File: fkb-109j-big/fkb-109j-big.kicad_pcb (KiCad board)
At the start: 2 copper layers, 260 parts

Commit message: continue layout
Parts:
- added MX_KPPLS2: MX-NoLED, Alps_Only:ALPS-2U, F.Cu at (602.5, 76.2)
- moved MX_KP1 264.0 mm to (545.3, 104.8)
- moved MX_KP2 264.0 mm to (564.4, 104.8)
- moved MX_KP3 264.0 mm to (583.4, 104.8)
- moved MX_KP7 264.0 mm to (545.3, 66.7)
- moved MX_KP8 264.0 mm to (564.4, 66.7)
- moved MX_KP9 264.0 mm to (583.4, 66.7)
- moved MX_KPDOT1 264.0 mm to (583.4, 123.8)
- moved MX_KPEQ1 264.0 mm to (564.4, 47.6)
- moved MX_KPFSL1 264.0 mm to (583.4, 47.6)
- moved MX_NMLK1 264.0 mm to (545.3, 47.6)
- moved MX_KP0 264.0 mm to (554.8, 123.8)
- moved MX_KP4 264.0 mm to (545.3, 85.7)
- moved MX_KP5 264.0 mm to (564.4, 85.7)
- moved MX_KP6 264.0 mm to (583.4, 85.7)
- moved MX_KPAST1 264.0 mm to (602.5, 47.6)
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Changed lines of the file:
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@@
   )
   (footprint "Alps_Only:ALPS-1U" (layer "F.Cu")
-    (at 438.15 -193.675)
+    (at 545.30625 47.625)
     (property "Sheetfile" "fkb-109j-big.kicad_sch")
     (property "Sheetname" "")
@@
   )
   (footprint "Alps_Only:ALPS-1U" (layer "F.Cu")
-    (at 444.5 80.9625)
+    (at 433.8955 80.9625)
     (property "Sheetfile" "fkb-109j-big.kicad_sch")
     (property "Sheetname" "")
@@
   )
   (footprint "Alps_Only:ALPS-1U" (layer "F.Cu")
-    (at 457.2 -174.625)
+    (at 564.35625 66.675)
     (property "Sheetfile" "fkb-109j-big.kicad_sch")
     (property "Sheetname" "")
@@
   )
   (footprint "Alps_Only:ALPS-1U" (layer "F.Cu")
-    (at 476.25 -136.525)
+    (at 583.40625 104.775)
     (property "Sheetfile" "fkb-109j-big.kicad_sch")
     (property "Sheetname" "")
@@
   )
   (footprint "Alps_Only:ALPS-1U" (layer "F.Cu")
-    (at 476.25 -174.625)
+    (at 583.40625 66.675)
     (property "Sheetfile" "fkb-109j-big.kicad_sch")
     (property "Sheetname" "")
@@
   )
   (footprint "Alps_Only:ALPS-1U" (layer "F.Cu")
-    (at 482.71875 138.14375)
+    (at 471.9955 138.1125)
     (property "Sheetfile" "fkb-109j-big.kicad_sch")
     (property "Sheetname" "")
@@
   )
   (footprint "Alps_Only:ALPS-1U" (layer "F.Cu")
-    (at 457.2 -193.675)
+    (at 564.35625 47.625)
     (property "Sheetfile" "fkb-109j-big.kicad_sch")
     (property "Sheetname" "")
@@
   )
   (footprint "Alps_Only:ALPS-1U" (layer "F.Cu")
-    (at 438.15 -136.525)
+    (at 545.30625 104.775)
     (property "Sheetfile" "fkb-109j-big.kicad_sch")
     (property "Sheetname" "")
@@
   )
   (footprint "Alps_Only:ALPS-1U" (layer "F.Cu")
-    (at 457.2 -136.525)
+    (at 564.35625 104.775)
     (property "Sheetfile" "fkb-109j-big.kicad_sch")
     (property "Sheetname" "")
@@
   )
   (footprint "Alps_Only:ALPS-1U" (layer "F.Cu")
-    (at 476.25 -117.475)
+    (at 583.40625 123.825)
     (property "Sheetfile" "fkb-109j-big.kicad_sch")
     (property "Sheetname" "")
@@
   )
   (footprint "Alps_Only:ALPS-1U" (layer "F.Cu")
-    (at 444.5 61.9125)
+    (at 433.8955 61.9125)
     (property "Sheetfile" "fkb-109j-big.kicad_sch")
     (property "Sheetname" "")
@@
   )
   (footprint "Alps_Only:ALPS-1U" (layer "F.Cu")
-    (at 463.55 80.9625)
+    (at 452.9455 80.9625)
     (property "Sheetfile" "fkb-109j-big.kicad_sch")
     (property "Sheetname" "")
@@
   )
   (footprint "Alps_Only:ALPS-1U" (layer "F.Cu")
-    (at 438.15 -174.625)
+    (at 545.30625 66.675)
     (property "Sheetfile" "fkb-109j-big.kicad_sch")
     (property "Sheetname" "")
@@
   )
   (footprint "Alps_Only:ALPS-2U" (layer "F.Cu")
-    (at 425.45 90.4875 -90)
+    (at 401.6375 109.5375 -90)
     (property "Sheetfile" "fkb-109j-big.kicad_sch")
     (property "Sheetname" "")
@@
   )
   (footprint "Alps_Only:ALPS-1U" (layer "F.Cu")
-    (at 463.66875 138.14375)
+    (at 452.9455 138.1125)
     (property "Sheetfile" "fkb-109j-big.kicad_sch")
     (property "Sheetname" "")
@@
   )
   (footprint "Alps_Only:ALPS-1U" (layer "F.Cu")
-    (at 476.25 -155.575)
+    (at 583.40625 85.725)
     (property "Sheetfile" "fkb-109j-big.kicad_sch")
     (property "Sheetname" "")
@@
     )
   )
+  (footprint "Alps_Only:ALPS-2U" (layer "F.Cu")
+    (at 602.45625 76.2 -90)
+    (property "Sheetfile" "fkb-109j-big.kicad_sch")
+    (property "Sheetname" "")
+    (attr through_hole)
+    (fp_text reference "MX_KPPLS2" (at 0 3.175 90) (layer "Dwgs.User")
+        (effects (font (size 1 1) (thickness 0.15)))
+    )
+    (fp_text value "MX-NoLED" (at 0 -7.9375 90) (layer "Dwgs.User")
+        (effects (font (size 1 1) (thickness 0.15)))
+    )
+    (fp_line (start -19.05 -9.525) (end 19.05 -9.525)
+      (stroke (width 0.15) (type solid)) (layer "Dwgs.User"))
+    (fp_line (start -19.05 9.525) (end -19.05 -9.525)
+      (stroke (width 0.15) (type solid)) (layer "Dwgs.User"))
+    (fp_line (start -19.05 9.525) (end 19.05 9.525)
+      (stroke (width 0.15) (type solid)) (layer "Dwgs.User"))
+    (fp_line (start -7 -7) (end -7 -5)
+      (stroke (width 0.15) (type solid)) (layer "Dwgs.User"))
+    (fp_line (start -7 5) (end -7 7)
+      (stroke (width 0.15) (type solid)) (layer "Dwgs.User"))
+    (fp_line (start -7 7) (end -5 7)
+      (stroke (width 0.15) (type solid)) (layer "Dwgs.User"))
+    (fp_line (start -5 -7) (end -7 -7)
+      (stroke (width 0.15) (type solid)) (layer "Dwgs.User"))
+    (fp_line (start 5 -7) (end 7 -7)
+      (stroke (width 0.15) (type solid)) (layer "Dwgs.User"))
+    (fp_line (start 5 7) (end 7 7)
+      (stroke (width 0.15) (type solid)) (layer "Dwgs.User"))
+    (fp_line (start 7 -7) (end 7 -5)
+      (stroke (width 0.15) (type solid)) (layer "Dwgs.User"))
+    (fp_line (start 7 7) (end 7 5)
+      (stroke (width 0.15) (type solid)) (layer "Dwgs.User"))
+    (fp_line (start 19.05 -9.525) (end 19.05 9.525)
+      (stroke (width 0.15) (type solid)) (layer "Dwgs.User"))
+    (pad "1" thru_hole circle (at -2.5 -4 270) (size 2.25 2.25) (drill 1.47) (layers "*.Cu" "B.Mask")
+      (net 160 "COL20") (pinfunction "COL") (pintype "passive"))
+    (pad "2" thru_hole circle (at 2.5 -4.5 270) (size 2.25 2.25) (drill 1.47) (layers "*.Cu" "B.Mask")
+      (net 126 "Net-(D111-A)") (pinfunction "ROW") (pintype "passive"))
+  )
   (footprint "Alps_Only:ALPS-1U" (layer "F.Cu")
     (at 173.0375 100.0125)
@@
   )
   (footprint "Alps_Only:ALPS-1U" (layer "F.Cu")
-    (at 457.2 -155.575)
+    (at 564.35625 85.725)
     (property "Sheetfile" "fkb-109j-big.kicad_sch")
     (property "Sheetname" "")
@@
   )
   (footprint "Alps_Only:ALPS-1U" (layer "F.Cu")
-    (at 463.66875 119.09375)
+    (at 452.9455 119.0625)
     (property "Sheetfile" "fkb-109j-big.kicad_sch")
     (property "Sheetname" "")
@@
   )
   (footprint "Alps_Only:ALPS-1U" (layer "F.Cu")
-    (at 463.55 61.9125)
+    (at 452.9455 61.9125)
     (property "Sheetfile" "fkb-109j-big.kicad_sch")
     (property "Sheetname" "")
@@
   )
   (footprint "Alps_Only:ALPS-1U" (layer "F.Cu")
-    (at 476.25 -193.675)
+    (at 583.40625 47.625)
     (property "Sheetfile" "fkb-109j-big.kicad_sch")
     (property "Sheetname" "")
@@
   )
   (footprint "Alps_Only:ALPS-1U" (layer "F.Cu")
-    (at 482.6 80.9625)
+    (at 471.9955 80.9625)
     (property "Sheetfile" "fkb-109j-big.kicad_sch")
     (property "Sheetname" "")
@@
   )
   (footprint "Alps_Only:ALPS-1U" (layer "F.Cu")
-    (at 495.3 -155.575)
+    (at 602.45625 85.725)
     (property "Sheetfile" "fkb-109j-big.kicad_sch")
     (property "Sheetname" "")
@@
   )
   (footprint "Alps_Only:ALPS-1U" (layer "F.Cu")
-    (at 482.6 61.9125)
+    (at 471.9955 61.9125)
     (property "Sheetfile" "fkb-109j-big.kicad_sch")
     (property "Sheetname" "")
@@
   )
   (footprint "Alps_Only:ALPS-1U" (layer "F.Cu")
-    (at 495.3 -193.675)
+    (at 602.45625 47.625)
     (property "Sheetfile" "fkb-109j-big.kicad_sch")
     (property "Sheetname" "")
@@
   )
   (footprint "Alps_Only:ALPS-2U" (layer "F.Cu")
-    (at 447.675 -117.475)
+    (at 554.83125 123.825)
     (property "Sheetfile" "fkb-109j-big.kicad_sch")
     (property "Sheetname" "")
@@
   )
   (footprint "Alps_Only:ALPS-2U" (layer "F.Cu")
-    (at 495.3 -127 -90)
+    (at 602.45625 114.3 -90)
     (property "Sheetfile" "fkb-109j-big.kicad_sch")
     (property "Sheetname" "")
@@
   )
   (footprint "Alps_Only:ALPS-1U" (layer "F.Cu")
-    (at 438.15 -155.575)
+    (at 545.30625 85.725)
     (property "Sheetfile" "fkb-109j-big.kicad_sch")
     (property "Sheetname" "")
@@
   )
   (footprint "Alps_Only:ALPS-1U" (layer "F.Cu")
-    (at 495.3 -174.625)
+    (at 602.45625 66.675)
     (property "Sheetfile" "fkb-109j-big.kicad_sch")
     (property "Sheetname" "")
@@
   )
   (footprint "Alps_Only:ALPS-1U" (layer "F.Cu")
-    (at 444.61875 138.14375)
+    (at 433.8955 138.1125)
     (property "Sheetfile" "fkb-109j-big.kicad_sch")
     (property "Sheetname" "")
@@
     )
   )
+  (dimension (type aligned) (layer "Dwgs.User")
+    (pts (xy 415.925 128.5875) (xy 424.3705 128.5875))
+    (height 0)
+    (gr_text "8.4455 mm" (at 420.14775 127.4375) (layer "Dwgs.User")
+      (effects (font (size 1 1) (thickness 0.15)))
+    )
+    (format (prefix "") (suffix "") (units 3) (units_format 1) (precision 4))
+    (style (thickness 0.15) (arrow_length 1.27) (text_position_mode 0) (extension_height 0.58642) (extension_offset 0.5) keep_text_aligned)
+  )
+  (dimension (type aligned) (layer "Dwgs.User")
+    (pts (xy 424.3705 147.6375) (xy 443.4205 147.6375))
+    (height 8.73125)
+    (gr_text "19.0500 mm" (at 433.8955 155.21875) (layer "Dwgs.User")
+      (effects (font (size 1 1) (thickness 0.15)))
+    )
+    (format (prefix "") (suffix "") (units 3) (units_format 1) (precision 4))
+    (style (thickness 0.15) (arrow_length 1.27) (text_position_mode 0) (extension_height 0.58642) (extension_offset 0.5) keep_text_aligned)
+  )
+  (dimension (type aligned) (layer "Dwgs.User")
+    (pts (xy 415.925 90.4875) (xy 424.3705 90.4875))
+    (height 0)
+    (gr_text "8.4455 mm" (at 420.14775 89.3375) (layer "Dwgs.User")
+      (effects (font (size 1 1) (thickness 0.15)))
+    )
+    (format (prefix "") (suffix "") (units 3) (units_format 1) (precision 4))
+    (style (thickness 0.15) (arrow_length 1.27) (text_position_mode 0) (extension_height 0.58642) (extension_offset 0.5) keep_text_aligned)
+  )
+  (dimension (type aligned) (layer "Dwgs.User")
+    (pts (xy 443.4205 90.4875) (xy 443.4205 109.5375))
+    (height -9.525)
+    (gr_text "19.0500 mm" (at 451.7955 100.0125 90) (layer "Dwgs.User")
+      (effects (font (size 1 1) (thickness 0.15)))
+    )
+    (format (prefix "") (suffix "") (units 3) (units_format 1) (precision 4))
+    (style (thickness 0.15) (arrow_length 1.27) (text_position_mode 0) (extension_height 0.58642) (extension_offset 0.5) keep_text_aligned)
+  )
   (segment (start 144.58125 133.6125) (end 146.9625 133.6125) (width 0.25) (layer "F.Cu") (net 24))

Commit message: finish preliminary layout
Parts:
- added MX_ESC2: MX-NoLED, Alps_Only:ALPS-1U, F.Cu at (139.7, 38.1)
- added MX_F14: MX-NoLED, Alps_Only:ALPS-1U, F.Cu at (177.8, 38.1)
- added MX_F15: MX-NoLED, Alps_Only:ALPS-1U, F.Cu at (196.8, 38.1)
- added MX_F16: MX-NoLED, Alps_Only:ALPS-1U, F.Cu at (215.9, 38.1)
- added MX_F17: MX-NoLED, Alps_Only:ALPS-1U, F.Cu at (234.9, 38.1)
- added MX_F18: MX-NoLED, Alps_Only:ALPS-1U, F.Cu at (263.5, 38.1)
- added MX_F19: MX-NoLED, Alps_Only:ALPS-1U, F.Cu at (282.6, 38.1)
- added MX_F20: MX-NoLED, Alps_Only:ALPS-1U, F.Cu at (301.6, 38.1)
- added MX_F21: MX-NoLED, Alps_Only:ALPS-1U, F.Cu at (320.7, 38.1)
- added MX_F22: MX-NoLED, Alps_Only:ALPS-1U, F.Cu at (349.2, 38.1)
- added MX_F23: MX-NoLED, Alps_Only:ALPS-1U, F.Cu at (368.3, 38.1)
- added MX_F24: MX-NoLED, Alps_Only:ALPS-1U, F.Cu at (387.4, 38.1)
- added MX_F25: MX-NoLED, Alps_Only:ALPS-1U, F.Cu at (406.4, 38.1)
- added MX_PSBRK2: MX-NoLED, Alps_Only:ALPS-1U, F.Cu at (473.1, 38.1)
- added MX_PSCRN2: MX-NoLED, Alps_Only:ALPS-1U, F.Cu at (435.0, 38.1)
- added MX_SCRLK2: MX-LED, Alps_Only:ALPS-1U, F.Cu at (454.0, 38.1)
- moved MX_PSBRK1 110.7 mm to (473.1, 38.1)
- moved MX_F9 83.2 mm to (349.2, 38.1), turned to 0 degrees
- moved MX_F10 82.0 mm to (368.3, 38.1), turned to 0 degrees
- moved MX_F11 80.9 mm to (387.4, 38.1), turned to 0 degrees
- moved MX_F12 79.8 mm to (406.4, 38.1), turned to 0 degrees
- moved MX_F5 78.4 mm to (263.5, 38.1), turned to 0 degrees
- moved MX_F6 77.2 mm to (282.6, 38.1), turned to 0 degrees
- moved MX_F7 76.1 mm to (301.6, 38.1), turned to 0 degrees
- moved MX_F8 75.0 mm to (320.7, 38.1), turned to 0 degrees
- moved MX_PSCRN1 67.6 mm to (435.0, 38.1)
- moved MX_SCRLK1 66.5 mm to (454.0, 38.1)
- moved MX_KP1 45.9 mm to (501.6, 119.1)
- moved MX_KP2 45.9 mm to (520.7, 119.1)
- moved MX_KP3 45.9 mm to (539.8, 119.1)
- moved MX_KP4 45.9 mm to (501.6, 100.0)
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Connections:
- MX_RSHFT1 pad 1: COL12 -> Net-(D77-A)
- MX_RSHFT1 pad 2: Net-(D77-A) -> COL12
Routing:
- net Net-(D4-A): track 0.00 -> 9.69 mm
- net Net-(D3-A): track 0.00 -> 9.69 mm
- net Net-(D2-A): track 0.00 -> 9.69 mm
- net Net-(D1-A): track 0.00 -> 9.69 mm
- net Net-(MX_F17-ROW): track 0.00 -> 2.62 mm
- net Net-(MX_F16-ROW): track 0.00 -> 2.62 mm
- net Net-(MX_F15-ROW): track 0.00 -> 2.62 mm
- net Net-(MX_F1-COL): track 0.00 -> 2.62 mm
- net Net-(MX_ESC1-COL): track 0.00 -> 2.62 mm
- net Net-(D25-A): track 0.00 -> 0.50 mm

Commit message: start moving diodes
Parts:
- added MX_BSLSH2: MX-NoLED, Alps_Only:ALPS-1U, F.Cu at (163.5, 119.1)
- added MX_LSHFT2: MX-NoLED, Alps_Only:ALPS-1.25U, F.Cu at (142.1, 119.1)
- moved D1 539.0 mm to (149.2, 47.5), turned to 90 degrees
- moved D5 537.0 mm to (149.2, 71.3), turned to 90 degrees
- moved D6 519.1 mm to (168.3, 71.3), turned to 90 degrees
- moved D2 502.6 mm to (187.3, 47.5), turned to 90 degrees
- moved D7 501.3 mm to (187.3, 71.3), turned to 90 degrees
- moved D3 485.0 mm to (206.4, 47.5), turned to 90 degrees
- moved D100 478.3 mm to (252.4, 202.0)
- moved D101 478.3 mm to (252.4, 205.5)
- moved D102 478.3 mm to (252.4, 209.1)
- moved D103 478.3 mm to (252.4, 212.6)
- moved D104 478.3 mm to (252.4, 216.2)
- moved D105 478.3 mm to (252.4, 219.7)
- moved D106 478.3 mm to (252.4, 223.3)
- moved D107 478.3 mm to (252.4, 226.8)
- moved D108 478.3 mm to (252.4, 230.4)
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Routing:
- net COL0: track 2.38 -> 52.2 mm
- net Net-(D17-A): track 0.00 -> 11.1 mm
- net Net-(D4-A): track 9.69 -> 0.50 mm
- net Net-(D3-A): track 9.69 -> 0.50 mm
- net Net-(D2-A): track 9.69 -> 0.50 mm
- net Net-(D1-A): track 9.69 -> 0.50 mm
- net Net-(D10-A): track 0.00 -> 2.38 mm

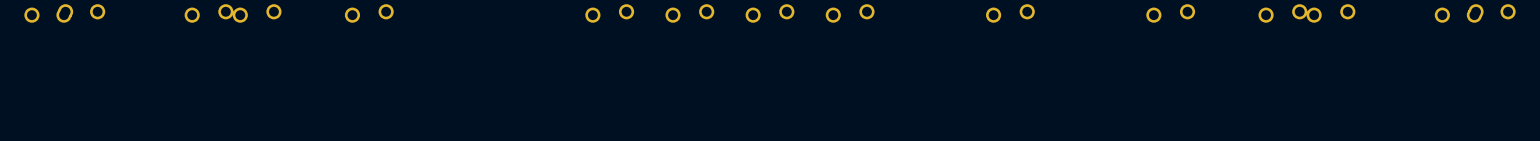
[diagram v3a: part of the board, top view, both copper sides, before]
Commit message: add 7u/jis bottom-row
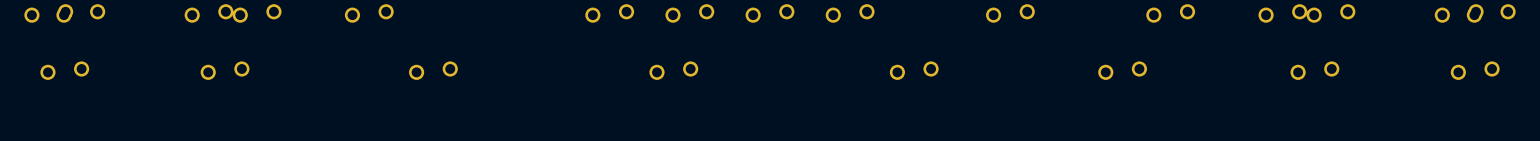
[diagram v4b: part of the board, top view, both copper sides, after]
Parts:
- added MX_KC1: MX-NoLED, Alps_Only:ALPS-1.5U, F.Cu at (325.4, 138.1)
- added MX_KC2: MX-NoLED, Alps_Only:ALPS-1.75U, F.Cu at (294.5, 138.1)
- added MX_KC7B2: MX-NoLED, Alps_Only:ALPS-1.75U, F.Cu at (223.0, 138.1)
- added MX_LALT2: MX-NoLED, Alps_Only:ALPS-1.5U, F.Cu at (192.1, 138.1)
- added MX_LWIN2: MX-NoLED, Alps_Only:ALPS-1U, F.Cu at (168.3, 138.1)
- added MX_RALT2: MX-NoLED, Alps_Only:ALPS-1.5U, F.Cu at (354.0, 138.1)
- added MX_RWIN2: MX-NoLED, Alps_Only:ALPS-1U, F.Cu at (377.8, 138.1)
- added MX_SPACE5: MX-NoLED, Alps_Only:ALPS-2U, F.Cu at (258.8, 138.1)

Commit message: continue placing diodes
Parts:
- moved D42 221.1 mm to (292.1, 46.7), turned to 90 degrees
- moved D54 211.1 mm to (330.2, 46.7), turned to 90 degrees
- moved D36 194.4 mm to (273.1, 46.7), turned to 90 degrees
- moved D37 192.5 mm to (263.5, 70.5), turned to 90 degrees
- moved D75 184.0 mm to (414.3, 127.6), turned to 90 degrees
- moved D48 183.1 mm to (311.1, 46.7), turned to 90 degrees
- moved D49 179.5 mm to (301.6, 70.5), turned to 90 degrees
- moved D50 170.7 mm to (311.1, 89.5), turned to 90 degrees
- moved D31 167.2 mm to (244.5, 70.5), turned to 90 degrees
- moved D30 166.2 mm to (244.5, 46.7), turned to 90 degrees
- moved D52 154.8 mm to (325.4, 127.6), turned to 90 degrees
- moved D32 154.5 mm to (254.0, 89.5), turned to 90 degrees
- moved D20 152.5 mm to (215.9, 89.5), turned to 90 degrees
- moved D43 152.0 mm to (282.6, 70.5), turned to 90 degrees
- moved D51 150.0 mm to (296.9, 108.6), turned to 90 degrees
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- renumbered D19 to D10, D87 to D100, D88 to D101, D89 to D102, D94 to D103, D95 to D104, D100 to D105, D109 to D108, D110 to D109, D20 to D11, D111 to D110, D112 to D111, D2 to D12, D7 to D13, D13 to D14, D14 to D15, D21 to D16, D22 to D17, D3 to D18, D8 to D19, D5 to D2, D15 to D20, D16 to D21, D23 to D22, D24 to D23, D4 to D24, D26 to D25, D27 to D26, D28 to D27, D29 to D28, D30 to D29, D9 to D3, D25 to D30, D32 to D31, D33 to D32, D34 to D33, D35 to D34, D36 to D35, D31 to D36, D38 to D37, D39 to D38, D40 to D39, D10 to D4, D41 to D40, D42 to D41, D37 to D42, D44 to D43, D45 to D44, D46 to D45, D47 to D46, D48 to D47, D43 to D48, D50 to D49, D17 to D5, D51 to D50, D52 to D51, D53 to D52, D54 to D53, D49 to D54, D56 to D55, D57 to D56, D58 to D57, D59 to D58, D60 to D59, D18 to D6, D55 to D60, D62 to D61, D63 to D62, D64 to D63, D65 to D64, D66 to D65, D61 to D66, D68 to D67, D69 to D68, D70 to D69, D6 to D7, D71 to D70, D67 to D71, D74 to D72, D75 to D73, D76 to D74, D77 to D75, D73 to D76, D79 to D77, D72 to D79, D11 to D8, D82 to D80, D91 to D81, D92 to D82, D93 to D83, D96 to D84, D97 to D85, D98 to D86, D99 to D87, D101 to D88, D102 to D89, D12 to D9, D103 to D90, D104 to D91, D105 to D92, D108 to D93, D80 to D94, D81 to D95, D83 to D96, D84 to D97, D85 to D98, D86 to D99

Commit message: finish preliminary diode placement.
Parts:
- moved D108 355.0 mm to (567.5, 70.5), turned to 90 degrees
- moved D103 354.6 mm to (548.5, 70.3), turned to 90 degrees
- moved D109 348.8 mm to (568.3, 89.5), turned to 90 degrees
- moved D104 347.7 mm to (549.3, 89.5), turned to 90 degrees
- moved D110 342.6 mm to (568.3, 108.4), turned to 90 degrees
- moved D111 329.2 mm to (566.7, 146.5), turned to 90 degrees
- moved D99 326.6 mm to (530.2, 70.3), turned to 90 degrees
- moved D100 319.6 mm to (530.2, 89.4), turned to 90 degrees
- moved D101 313.3 mm to (530.2, 108.4), turned to 90 degrees
- moved D106 311.9 mm to (549.3, 127.6), turned to 90 degrees
- moved D105 311.2 mm to (549.3, 108.4), turned to 90 degrees
- moved D102 307.5 mm to (530.2, 127.6), turned to 90 degrees
- moved D107 307.5 mm to (549.3, 146.7), turned to 90 degrees
- moved D94 299.9 mm to (511.2, 70.3), turned to 90 degrees
- moved D98 296.1 mm to (528.6, 146.7), turned to 90 degrees
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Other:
- board outline added: 438.2 x 119.1 mm

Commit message: panelize all the things
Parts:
- added mouse-bite-5mm-slot: VAL**, Panelization:mouse-bite-5mm-slot, F.Cu at (418.4, 71.5)
- added mouse-bite-5mm-slot: VAL**, Panelization:mouse-bite-5mm-slot, F.Cu at (149.2, 49.9)
- added mouse-bite-5mm-slot: VAL**, Panelization:mouse-bite-5mm-slot, F.Cu at (449.5, 49.9)
- added mouse-bite-5mm-slot: VAL**, Panelization:mouse-bite-5mm-slot, F.Cu at (273.1, 49.9)
- added mouse-bite-5mm-slot: VAL**, Panelization:mouse-bite-5mm-slot, F.Cu at (418.4, 37.8)
- added mouse-bite-5mm-slot: VAL**, Panelization:mouse-bite-5mm-slot, F.Cu at (480.6, 128.6)
- added mouse-bite-5mm-slot: VAL**, Panelization:mouse-bite-5mm-slot, F.Cu at (418.4, 128.6)
- added mouse-bite-5mm-slot: VAL**, Panelization:mouse-bite-5mm-slot, F.Cu at (480.6, 71.4)
- added mouse-bite-5mm-slot: VAL**, Panelization:mouse-bite-5mm-slot, F.Cu at (396.9, 49.9)
- moved D76 11.9 mm to (403.2, 46.1), turned to 0 degrees
- moved D100 9.05 mm to (521.2, 89.4)
- moved D101 9.05 mm to (521.2, 108.4)
- moved D102 9.05 mm to (521.2, 127.6)
- moved D103 9.05 mm to (539.4, 70.3)
- moved D109 9.05 mm to (559.3, 89.5)
- moved D110 9.05 mm to (559.3, 108.4)
- moved D98 9.05 mm to (519.6, 146.7)
- moved D99 9.05 mm to (521.2, 70.3)
- moved MX_KP2 9.05 mm to (511.6, 119.1)
- moved MX_KP5 9.05 mm to (511.6, 100.0)
- moved MX_KP8 9.05 mm to (511.6, 81.0)
- moved MX_KPEQ1 9.05 mm to (511.6, 61.9)
- moved D94 9.05 mm to (502.1, 70.3)
- moved D95 9.05 mm to (502.1, 89.4)
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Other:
- board size 438.2 x 119.1 mm -> 429.1 x 119.3 mm
- board text added: "Offset: (5-19.05/4) mm"

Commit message: layout cont.
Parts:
- removed R1, R10, R11, R12, R13, R17, R18, R19, R2, R20, R21, R22, R3, R4, R5, R6, R7, R8, R9: R, Resistor_THT:R_Axial_DIN0207_L6.3mm_D2.5mm_P10.16mm_Horizontal
- added J1: Conn_02x07_Counter_Clockwise, Connector_PinHeader_2.00mm:PinHeader_1x14_P2.00mm_Vertical, F.Cu at (171.6, 53.9)
- added J2: Conn_02x07_Counter_Clockwise, Connector_PinHeader_2.00mm:PinHeader_1x14_P2.00mm_Vertical, F.Cu at (171.6, 46.1)
- added J3: Conn_01x01_Pin, Connector_PinHeader_2.00mm:PinHeader_1x01_P2.00mm_Vertical, F.Cu at (414.4, 46.0)
- added J4: Conn_01x01_Pin, Connector_PinHeader_2.00mm:PinHeader_1x01_P2.00mm_Vertical, F.Cu at (422.6, 46.0)
- added J5: Conn_01x05_Pin, Connector_PinHeader_2.00mm:PinHeader_1x05_P2.00mm_Vertical, F.Cu at (414.1, 54.0)
- moved R23 239.3 mm to (450.3, 222.3)
- moved R24 239.3 mm to (450.3, 226.3)
- moved R25 239.3 mm to (450.3, 230.4)
- moved R26 239.3 mm to (450.3, 234.4)
- moved R14 225.9 mm to (450.3, 210.2)
- moved R15 225.9 mm to (450.3, 214.2)
- moved R16 225.9 mm to (450.3, 218.2)
- moved D12 31.3 mm to (160.7, 30.0), turned to 0 degrees
- moved D48 21.3 mm to (292.0, 37.1)
- moved D60 21.3 mm to (339.7, 37.1)
- moved D36 21.2 mm to (254.0, 37.1)
- moved D42 21.2 mm to (273.1, 37.1)
- moved D54 21.2 mm to (311.1, 37.1)
- moved D24 21.2 mm to (206.4, 37.1)
- moved D30 21.2 mm to (225.4, 37.1)
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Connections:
- net COL0 renamed COL0_BOTTOM
- net COL1 renamed COL1_BOTTOM
- net COL10 renamed COL10_BOTTOM
- net COL11 renamed COL11_BOTTOM
- net COL12 renamed COL12_BOTTOM
- net COL13 renamed COL13_BOTTOM
- net COL14 renamed COL14_BOTTOM
- net COL15 renamed COL15_BOTTOM
- net COL16 renamed COL16_BOTTOM
- net COL17 renamed COL17_BOTTOM
- net COL18 renamed COL18_BOTTOM
- net COL19 renamed COL19_BOTTOM
- net COL2 renamed COL2_BOTTOM
- net COL20 renamed COL20_BOTTOM
- net COL3 renamed COL3_BOTTOM
- net COL4 renamed COL4_BOTTOM
- net COL5 renamed COL5_BOTTOM
- net COL6 renamed COL6_BOTTOM
- net COL7 renamed COL7_BOTTOM
- net COL8 renamed COL8_BOTTOM
- net COL9 renamed COL9_BOTTOM
- net Net-(MX_ESC1-COL) renamed COL0_TOP
- net Net-(MX_F1-COL) renamed COL2_TOP
- net Net-(MX_F10-COL) renamed COL11_TOP
- net Net-(MX_F11-COL) renamed COL12_TOP
- net Net-(MX_F12-COL) renamed COL13_TOP
- net Net-(MX_F15-ROW) renamed COL3_TOP
- net Net-(MX_F16-ROW) renamed COL4_TOP
- net Net-(MX_F17-ROW) renamed COL5_TOP
- net Net-(MX_F18-ROW) renamed COL6_TOP
- net Net-(MX_F19-ROW) renamed COL7_TOP
- net Net-(MX_F20-ROW) renamed COL8_TOP
- net Net-(MX_F21-ROW) renamed COL9_TOP
- net Net-(MX_F22-ROW) renamed COL10_TOP
- net ROW0 renamed ROW0_LEFT
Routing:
- net ROW5: track 0.00 -> 346.5 mm
- net ROW4: track 0.00 -> 326.3 mm
- net ROW0_LEFT: track 0.00 -> 304.0 mm
- net ROW3: track 0.00 -> 298.1 mm
- net ROW2: track 0.00 -> 273.9 mm
- net ROW1: track 0.00 -> 271.8 mm
- net COL10_BOTTOM: track 2.38 -> 263.6 mm
- net COL13_BOTTOM: track 0.00 -> 258.5 mm
- net COL12_BOTTOM: track 0.00 -> 244.2 mm
- net COL8_BOTTOM: track 2.35 -> 245.7 mm
- net COL9_BOTTOM: track 0.60 -> 243.1 mm
- net COL7_BOTTOM: track 0.00 -> 222.2 mm
- net COL11_BOTTOM: track 0.00 -> 221.9 mm
- net COL13_TOP: track 0.00 -> 211.4 mm
- net COL6_BOTTOM: track 0.00 -> 200.4 mm
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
